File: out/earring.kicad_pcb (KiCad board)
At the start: 4 copper layers, 30.5 x 35.8 mm, 167 parts, among them J1 USB-C, Q1 ALS-PT19, Q10 BSS138W, Q2 CJ2101, Q3 BSS138W, Q4 LBSS84WT1G, Q5 BSS138W, Q6 BSS138W, Q7 BSS138W, Q8 CJ2101, Q9 BSS138W, SW2 PWR, U1 RP2350A, U10 TPS22913, U2 LGS4056H, U3 NCP730-3.3, U4 TPS22913, U5 USBLC6-2P6, U6 LSM6DS3TR-C, U7 W25Q16JVUXIQ, U8 74LVC2G14, U9 TPS22913, Y1 12MHz

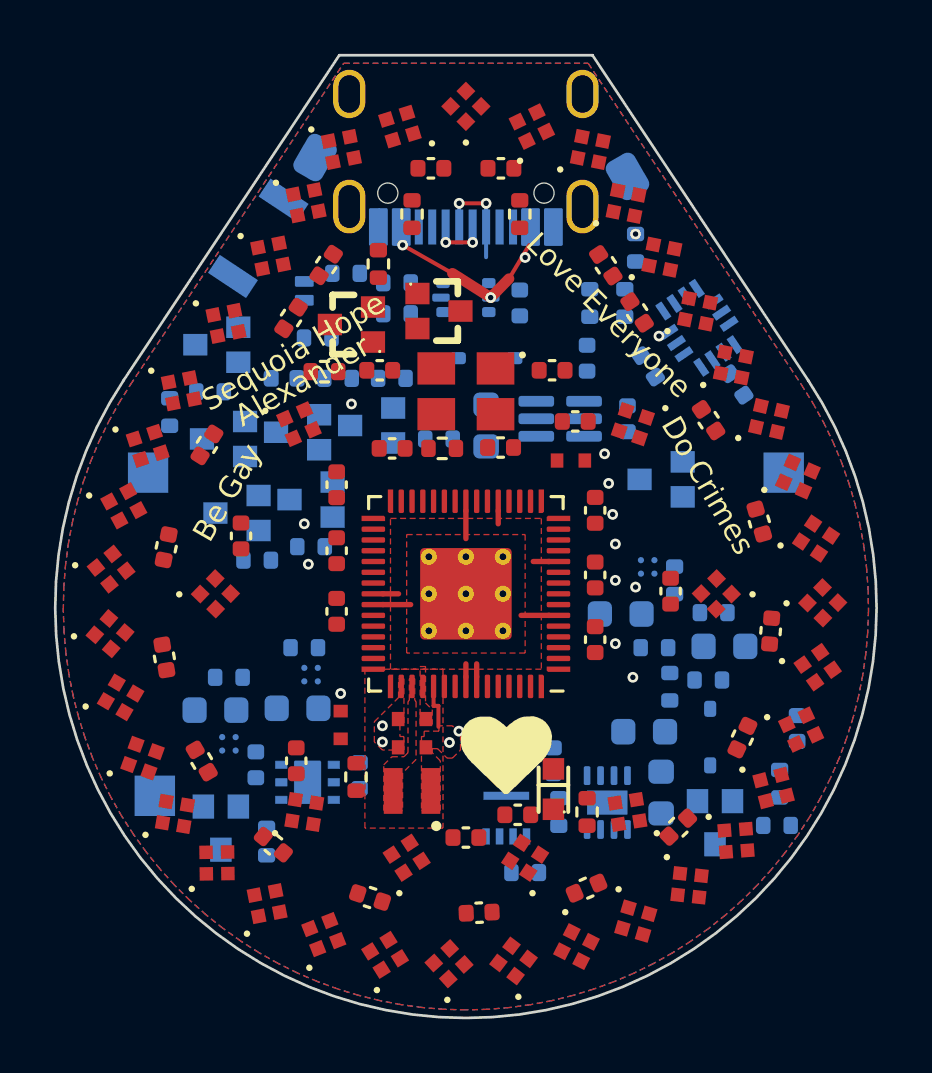
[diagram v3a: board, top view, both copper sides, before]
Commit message: Route with ultraroute; widen the LED supply tracks to 0.3 mm
The board is now routed by ultraroute (lab vled-width-1, seed 0) instead
of the freerouting-era route.

- VLED_L/C/R get their own "vled" net class: 0.3 mm tracks, with a
  .kicad_dru rule that allows narrowing to no less than 0.2 mm at the
  LED pads. They were on the 0.15 mm default. The In2 pours are cut
  into pieces joined by tracks, so ring current runs on tracks too.
- Routed with --planes In1.Cu (In1 stays a solid GND plane, one piece)
  and --pour-cost 3 (signals avoid cutting In2's VLED and 3V3 pours).
- route.py drops the freerouting assist vias and stubs that dangled once
  their unlocked tracks were stripped; R14's 3V3 via-in-pad is 6-layer
  only. Two locked 3V3 access vias this route left unused were removed
  from the board.

KiCad DRC: 0 errors, 0 unconnected, 0 dangling (67 silk/library
warnings). Schematic parity: the 28 known items only. No part moved.
USB pair 24.6 / 24.5 mm, still partly uncoupled.

Co-Authored-By: Claude Opus 5.5 <noreply@anthropic.com>
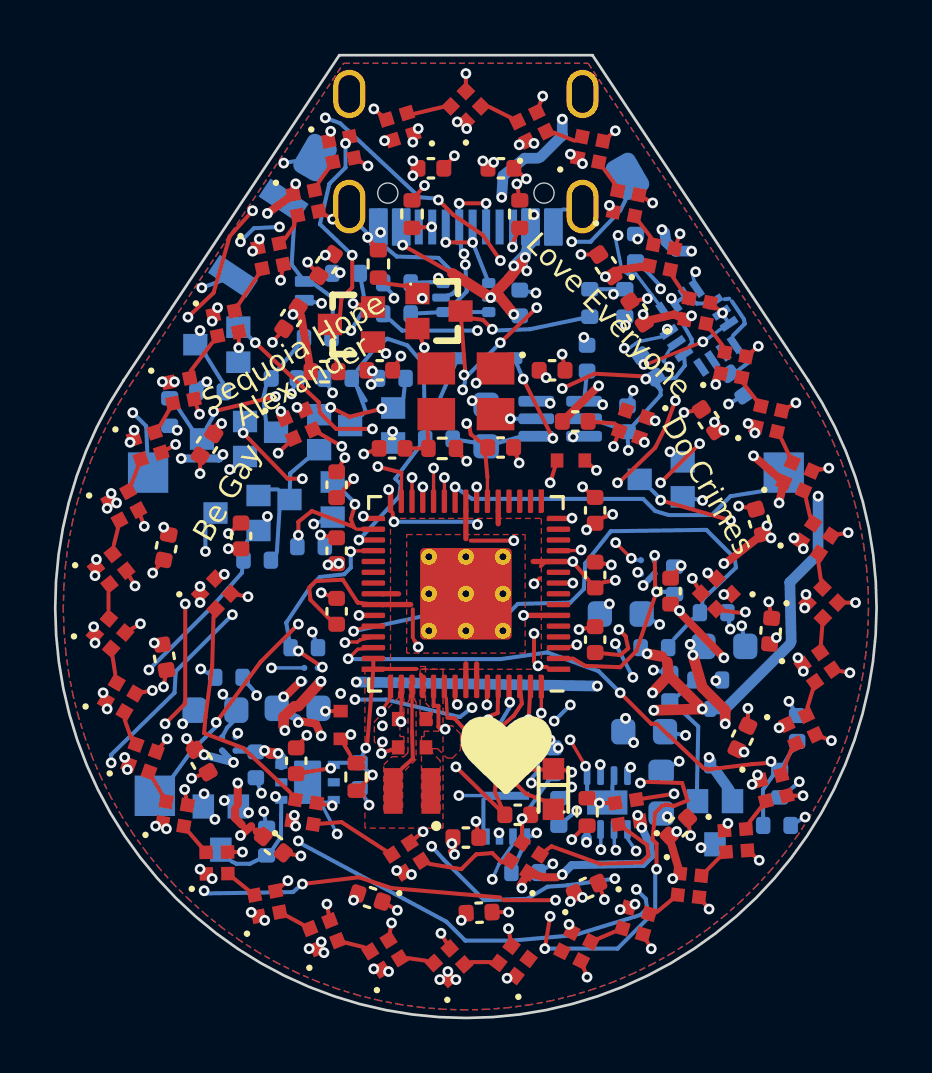
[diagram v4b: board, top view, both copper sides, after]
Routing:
- net GND: track 0.00 -> 100.2 mm, vias 3 -> 129
- net 3V3: track 2.69 -> 77.0 mm, vias 7 -> 34
- net VLED_R: track 0.00 -> 68.8 mm, vias 0 -> 48
- net VLED_L: track 0.00 -> 65.2 mm, vias 0 -> 50
- net VLED_C: track 0.00 -> 65.1 mm, vias 0 -> 26
- net VBATT: track 0.00 -> 57.2 mm, vias 0 -> 10
- net VBUS: track 6.24 -> 59.6 mm, vias 3 -> 22
- net RUN: track 0.00 -> 44.8 mm, vias 0 -> 12
- net SW_ON: track 0.00 -> 38.0 mm, vias 0 -> 6
- net CHRG: track 0.00 -> 37.0 mm, vias 0 -> 7
- net BOOTSEL_SW: track 0.00 -> 30.3 mm, vias 0 -> 7
- net VSYS: track 0.00 -> 27.8 mm, vias 0 -> 11
- net PWR_EN: track 0.00 -> 27.3 mm, vias 0 -> 2
- net USB_DM: track 0.00 -> 24.6 mm, vias 1 -> 2
- net USB_DP: track 0.00 -> 24.5 mm, vias 1 -> 2
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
